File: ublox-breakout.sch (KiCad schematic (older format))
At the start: 26 parts, among them J1 Conn_01x08, J2 Conn_01x08, J3 Conn_Coaxial, J4 USB_B_Micro, U1 LK112M33TR, U2 UBLOX_NEO-M8T-0, U3 USBLC6-2SC6, U4 LK112M33TR

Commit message: Prototype LEA-M8 breakout board
includes fabrication Gerber files and BOM+CPL files for
JLCPCB SMT service.

PCB must be ordered with impedance control JLC7628 stack-up
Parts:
- removed J1, J2: Conn_01x08, Connector_PinSocket_2.54mm:PinSocket_1x08_P2.54mm_Vertical, symbol Connector_Generic:Conn_01x08
- removed L1: 27nH, Inductor_SMD:L_0805_2012Metric, symbol Device:L_Small
- removed U1, U4: LK112M33TR, Package_TO_SOT_SMD:SOT-23-5, symbol Regulator_Linear:LK112M33TR
- removed U2: UBLOX_NEO-M8T-0, project:UBLOX_NEO-M8T-0, symbol project:UBLOX_NEO-M8T-0
- added D1: B5819W, Diode_SMD:D_SOD-123, symbol Device:D_Schottky_Small
- added D2: LED Green, LED_SMD:LED_0603_1608Metric, symbol Device:LED_Small
- added D3: LED Red, LED_SMD:LED_0603_1608Metric, symbol Device:LED_Small
- added H1, H2, H3, H4: MountingHole_Pad, MountingHole:MountingHole_2.2mm_M2_Pad_Via, symbol Mechanical:MountingHole_Pad
- added J1: Conn_02x06_Odd_Even, Connector_PinHeader_2.54mm:PinHeader_2x06_P2.54mm_Vertical, symbol Connector_Generic:Conn_02x06_Odd_Even
- added R10, R11: 27, Resistor_SMD:R_0603_1608Metric, symbol Device:R_Small
- added R12, R13: 620, Resistor_SMD:R_0603_1608Metric, symbol Device:R_Small
- added U1: ME6211C33M5G-N, Package_TO_SOT_SMD:SOT-23-5, symbol Regulator_Linear:APE8865Y5-33-HF-3
- added U2: UBLOX_LEA-M8T-0, RF_GPS:ublox_LEA, symbol project:UBLOX_LEA-M8T-0
- added U4: XC6206P332MR, Package_TO_SOT_SMD:SOT-23, symbol Regulator_Linear:XC6206PxxxMR
- C1, C3, C8: footprint Capacitor_SMD:C_0805_2012Metric -> Capacitor_SMD:C_0603_1608Metric; JLCPN (none) -> C15849
- C2: footprint Capacitor_SMD:C_0805_2012Metric -> Capacitor_SMD:C_0603_1608Metric; JLCPN (none) -> C14663
- C4, C7: value 100n -> 1u; footprint Capacitor_SMD:C_0805_2012Metric -> Capacitor_SMD:C_0603_1608Metric; JLCPN (none) -> C15849
- C5: footprint Capacitor_SMD:C_0805_2012Metric -> Capacitor_SMD:C_0603_1608Metric; JLCPN (none) -> C57112; MPN (none) -> 0603B103K500NT
- C6: value 1u -> 100n; footprint Capacitor_SMD:C_0805_2012Metric -> Capacitor_SMD:C_0603_1608Metric; JLCPN (none) -> C14663
- R1, R2, R3, R8: value 22 -> 27; footprint Resistor_SMD:R_0805_2012Metric -> Resistor_SMD:R_0603_1608Metric; JLCPN (none) -> C25190
- R4: footprint Resistor_SMD:R_0805_2012Metric -> Resistor_SMD:R_0603_1608Metric; JLCPN (none) -> C22859
- R5, R6: footprint Resistor_SMD:R_0805_2012Metric -> Resistor_SMD:R_0603_1608Metric; JLCPN (none) -> C25190
- R7: value 100k -> 62k; footprint Resistor_SMD:R_0805_2012Metric -> Resistor_SMD:R_0603_1608Metric; JLCPN (none) -> C23221
- R9: value 100k -> 110k; footprint Resistor_SMD:R_0805_2012Metric -> Resistor_SMD:R_0603_1608Metric; JLCPN (none) -> C25805
- U3: JLCPN (none) -> C7519
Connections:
- net labels added: EXTINT0, EXTINT1, SCL, SDA, TIMEPULSE, TIMEPULSE2, USB_D+, USB_D-
- net labels removed: GPS_1PPS, GPS_RESET_N, USB_DM, USB_DP
- wire segments 107 -> 126
- no-connect marks 8 -> 6
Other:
- moved on the sheet: C1, C2, C3, C4, C5, J3, J4, R1, R2, R3, R4, R5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

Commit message: Update LEA breakout board:
- add backup battery
- add buffered PPS output
- add pull-up resistors for SCL/SDA
- add D_SEL on pin header
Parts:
- removed C2: 100n, Capacitor_SMD:C_0603_1608Metric, symbol Device:C_Small
- removed C3: 1u, Capacitor_SMD:C_0603_1608Metric, symbol Device:C_Small
- removed U1: ME6211C33M5G-N, Package_TO_SOT_SMD:SOT-23-5, symbol Regulator_Linear:APE8865Y5-33-HF-3
- added BT1: Battery_Cell, Battery:BatteryHolder_Keystone_3000_1x12mm, symbol Device:Battery_Cell
- added D4, D5: 1N4148WS, Diode_SMD:D_SOD-323, symbol Diode:1N4148WS
- added J2: Conn_Coaxial, Connector_Coaxial:SMA_Amphenol_132134_Vertical, symbol Connector:Conn_Coaxial
- added R14, R15: 4k7, Resistor_SMD:R_0603_1608Metric, symbol Device:R_Small
- added R16, R17: 82, Resistor_SMD:R_0603_1608Metric, symbol Device:R_Small
- added U1: 74HCT2G125DP,125, Package_SO:VSSOP-8_3.0x3.0mm_P0.65mm, symbol 74xGxx:74AUC2G125
- C1: value 1u -> 100n; JLCPN C15849 -> C14663
- U3: value USBLC6-2SC6 -> TPUSBLC6-2SC6; JLCPN C7519 -> C558442
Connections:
- net labels added: D_SEL, PPS_OUT, V_BKP
- wire segments 126 -> 144
- no-connect marks 6 -> 4
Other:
- moved on the sheet: C4, C6, C7, C8, D1, D2, J4, R1, R12, R7, R9, U3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

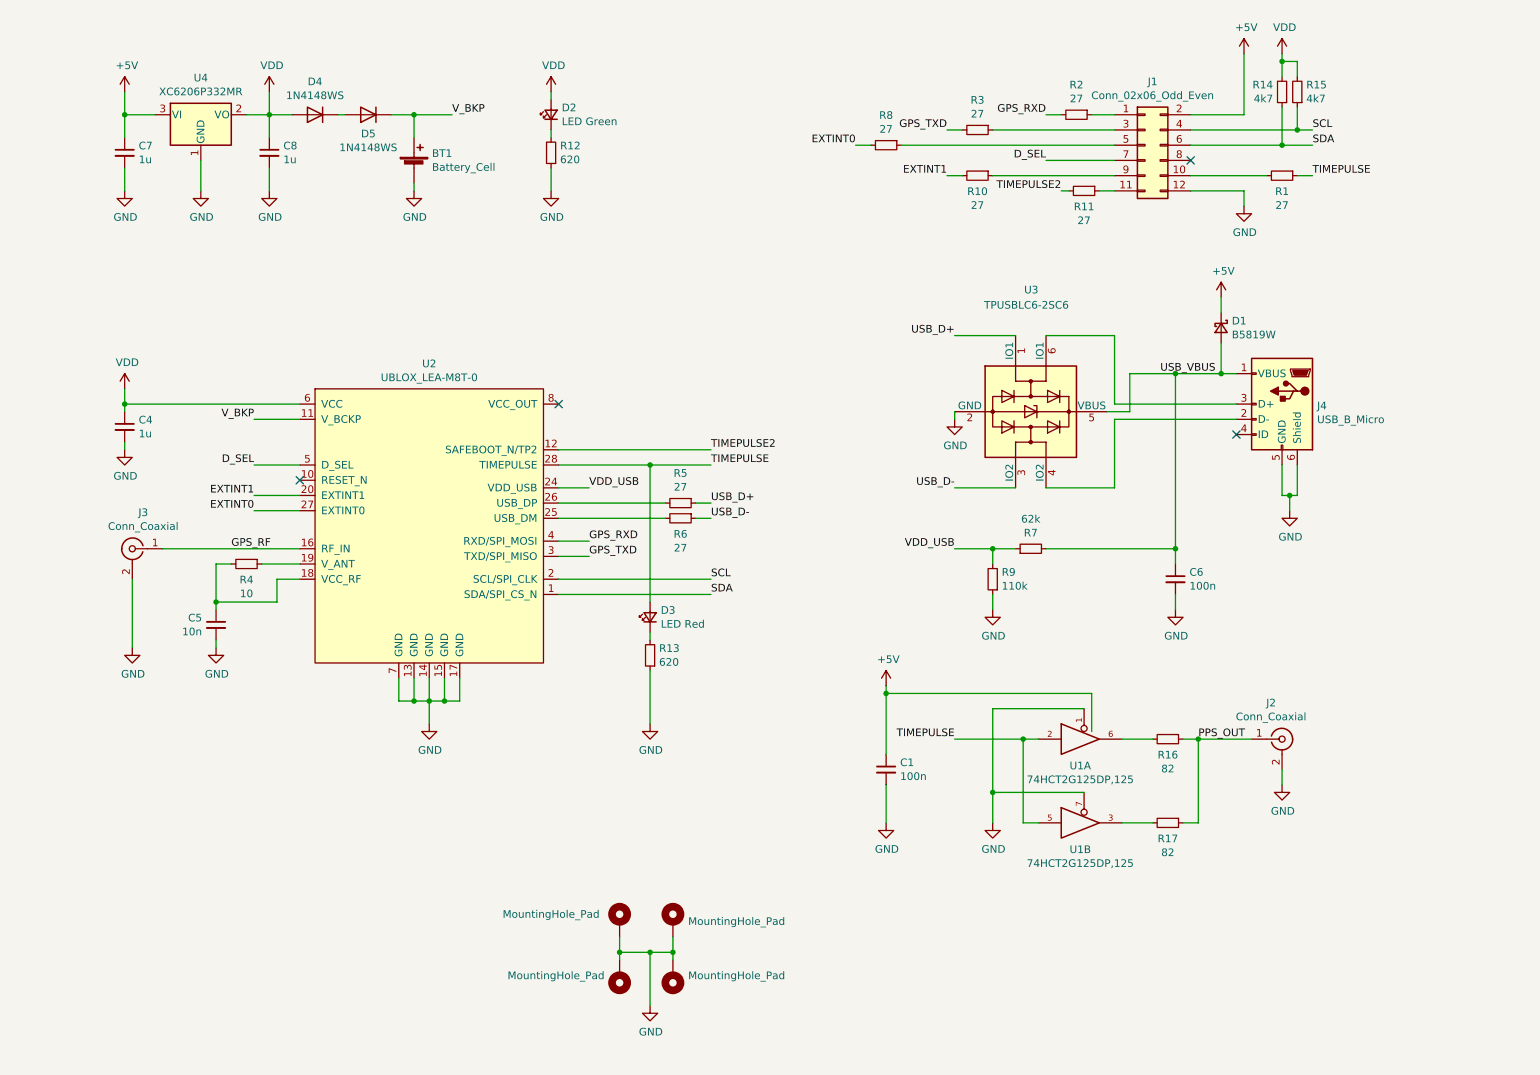
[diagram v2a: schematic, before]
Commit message: BOM and schematic updates
- mark I2C pull-ups DNP (module has built-in pull resistors)
- small schematic cleanups
- add schematic PDF and board image
- update fabrication data
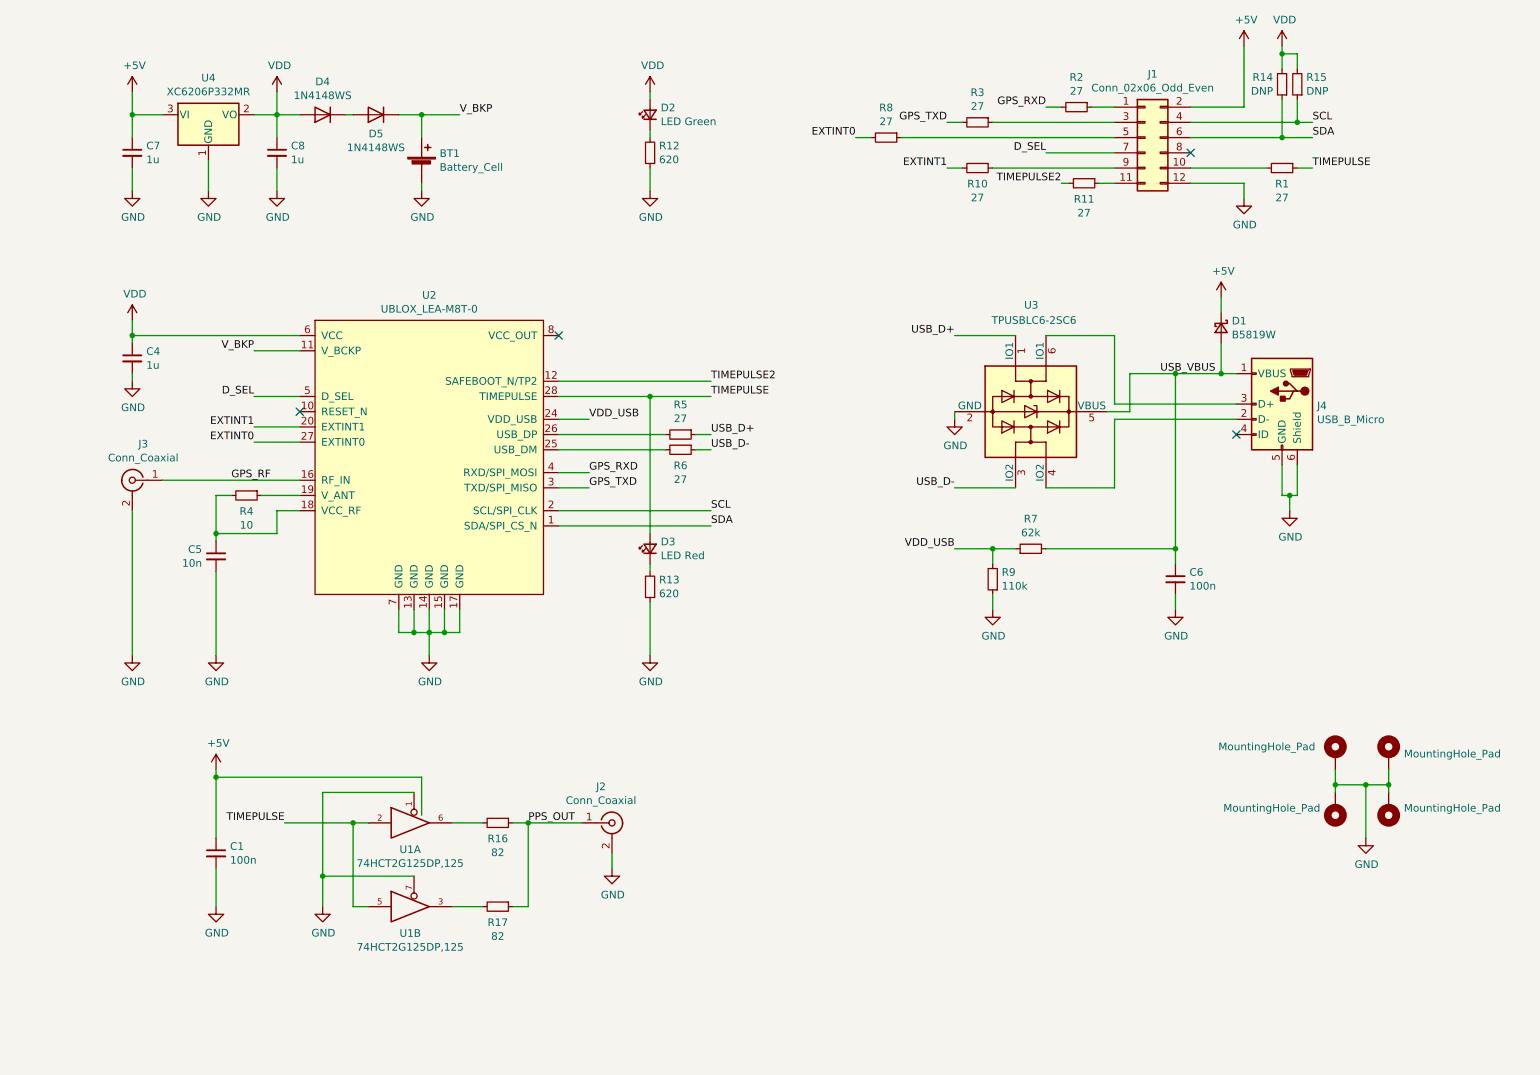
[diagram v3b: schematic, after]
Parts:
- R14, R15: value 4k7 -> DNP; JLCPN C23162 -> (none)
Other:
- moved on the sheet: BT1, C1, C4, C5, C7, C8, D2, D3, D4, D5, J1, J2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

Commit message: PCB and schematic updates
- change backup battery circuit to prevent inverse current
- add bulk capacitor to +5V rail
- add ESD protection diode for RF input
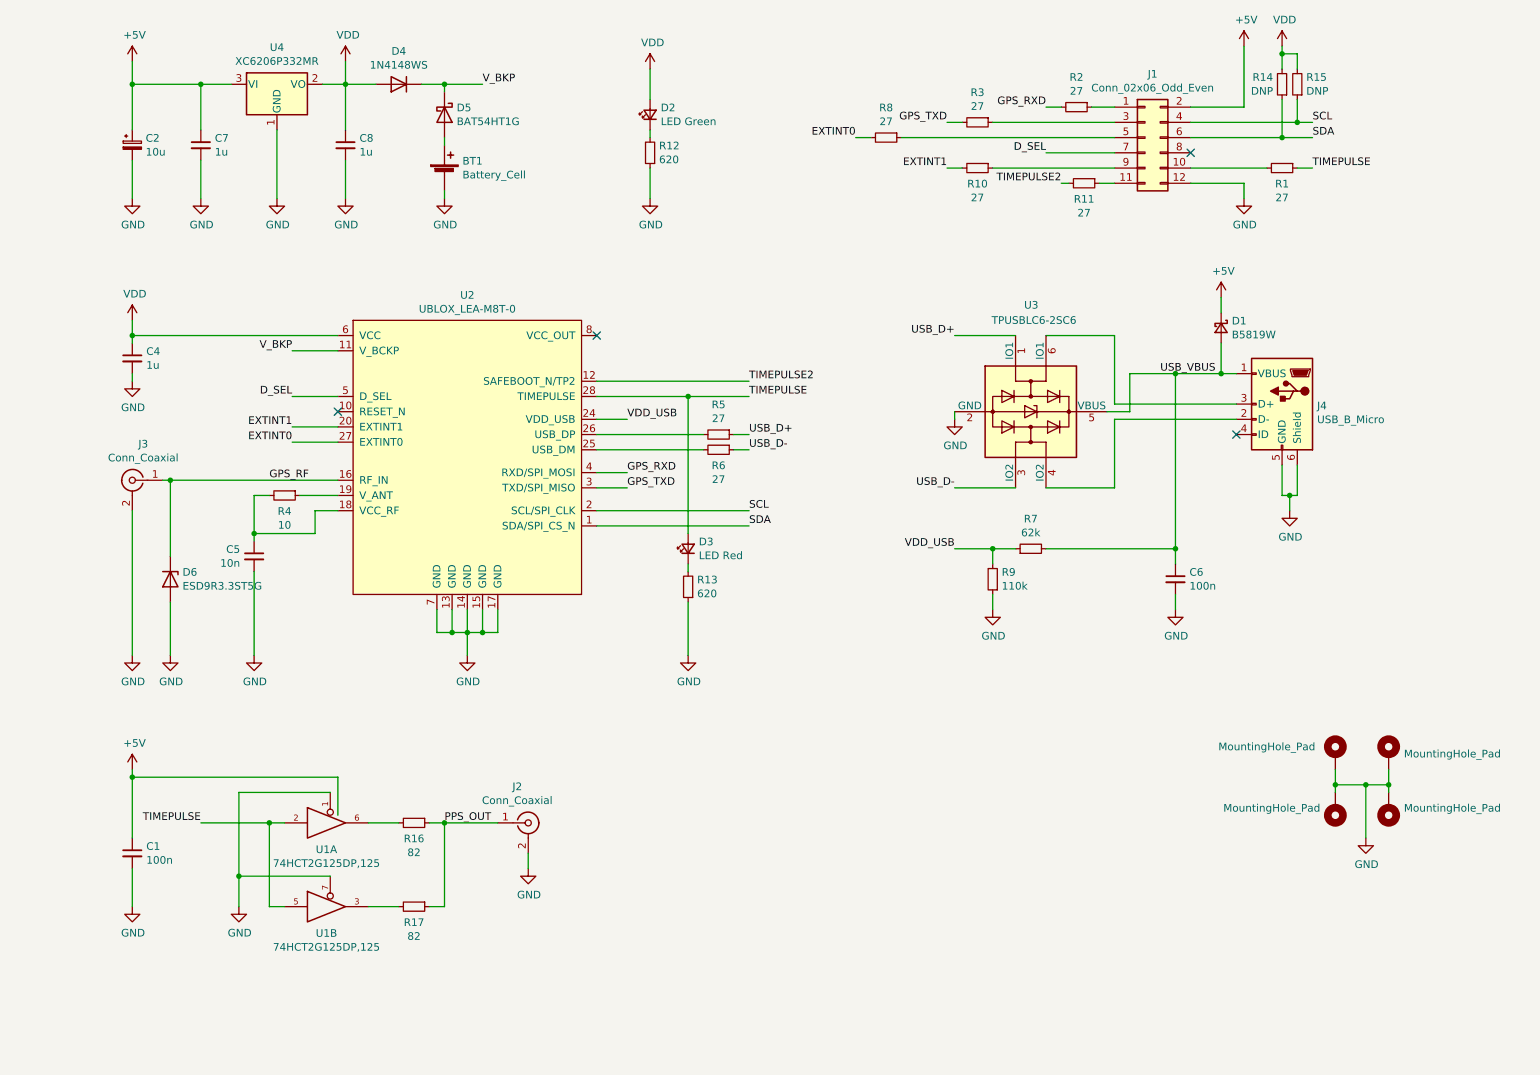
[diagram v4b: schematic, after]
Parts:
- removed D5: 1N4148WS, Diode_SMD:D_SOD-323, symbol Diode:1N4148WS
- added C2: 10u, Capacitor_Tantalum_SMD:CP_EIA-3216-18_Kemet-A, symbol Device:CP_Small
- added D5: BAT54HT1G, Diode_SMD:D_SOD-323, symbol Device:D_Schottky
- added D6: ESD9R3.3ST5G, Diode_SMD:D_SOD-923, symbol Device:D_Zener
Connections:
- net +5V: now also C2.1
- net GND: now also C2.2, D6.2 (A)
- net GPS_RF: now also D6.1 (K)
- net V_BKP: now also D4.1 (K), D5.1 (K); no longer BT1.1 (+)
- new net: BT1.1 (+), D5.2 (A)
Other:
- moved on the sheet: BT1, C1, C5, C7, C8, D3, D4, J2, R13, R16, R17, R4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
